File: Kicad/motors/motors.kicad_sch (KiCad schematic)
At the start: 6 parts

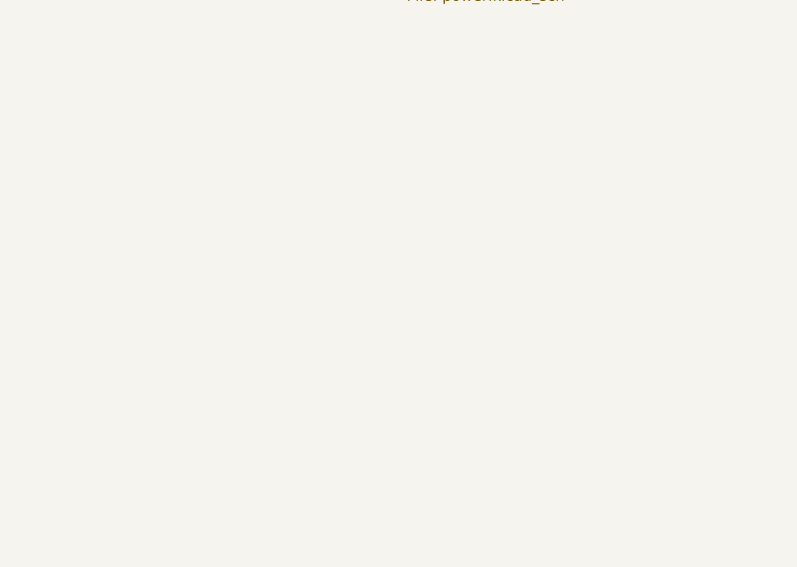
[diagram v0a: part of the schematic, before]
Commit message: Update Motors
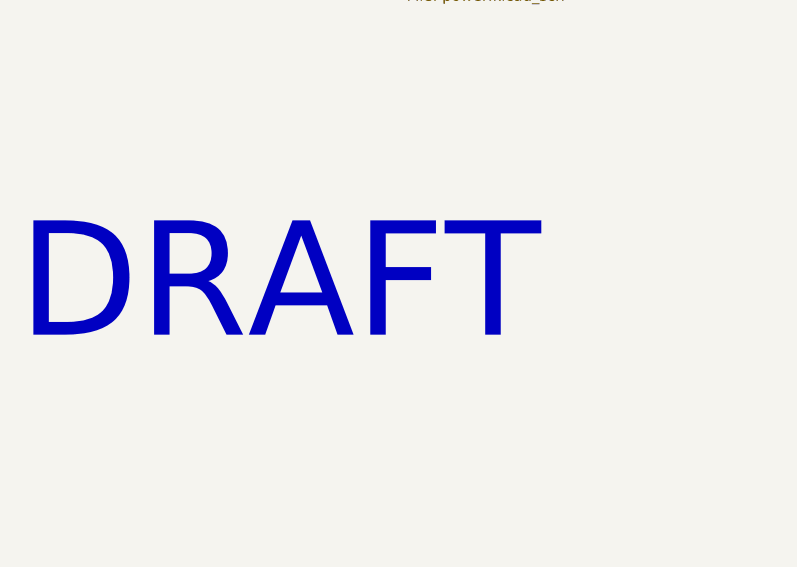
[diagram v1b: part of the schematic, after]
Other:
- note added: "DRAFT"
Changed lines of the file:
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@@
     (comment 1 "TCAR Motor Board - L298P")
+  )
+  (text "DRAFT" (at 66.04 137.16 0)
+    (effects (font (size 12.7 12.7)) (justify left bottom))
   )
   (symbol (lib_id "tronixio:MOUNTING-HOLE-MASK-3MM") (at 276.86 172.72 0) (unit 1)

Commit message: Update Motor
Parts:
- added H? (x10): MOUNTING-HOLE-MASK-3MM, tronixio:M3-MASK, symbol tronixio:MOUNTING-HOLE-MASK-3MM

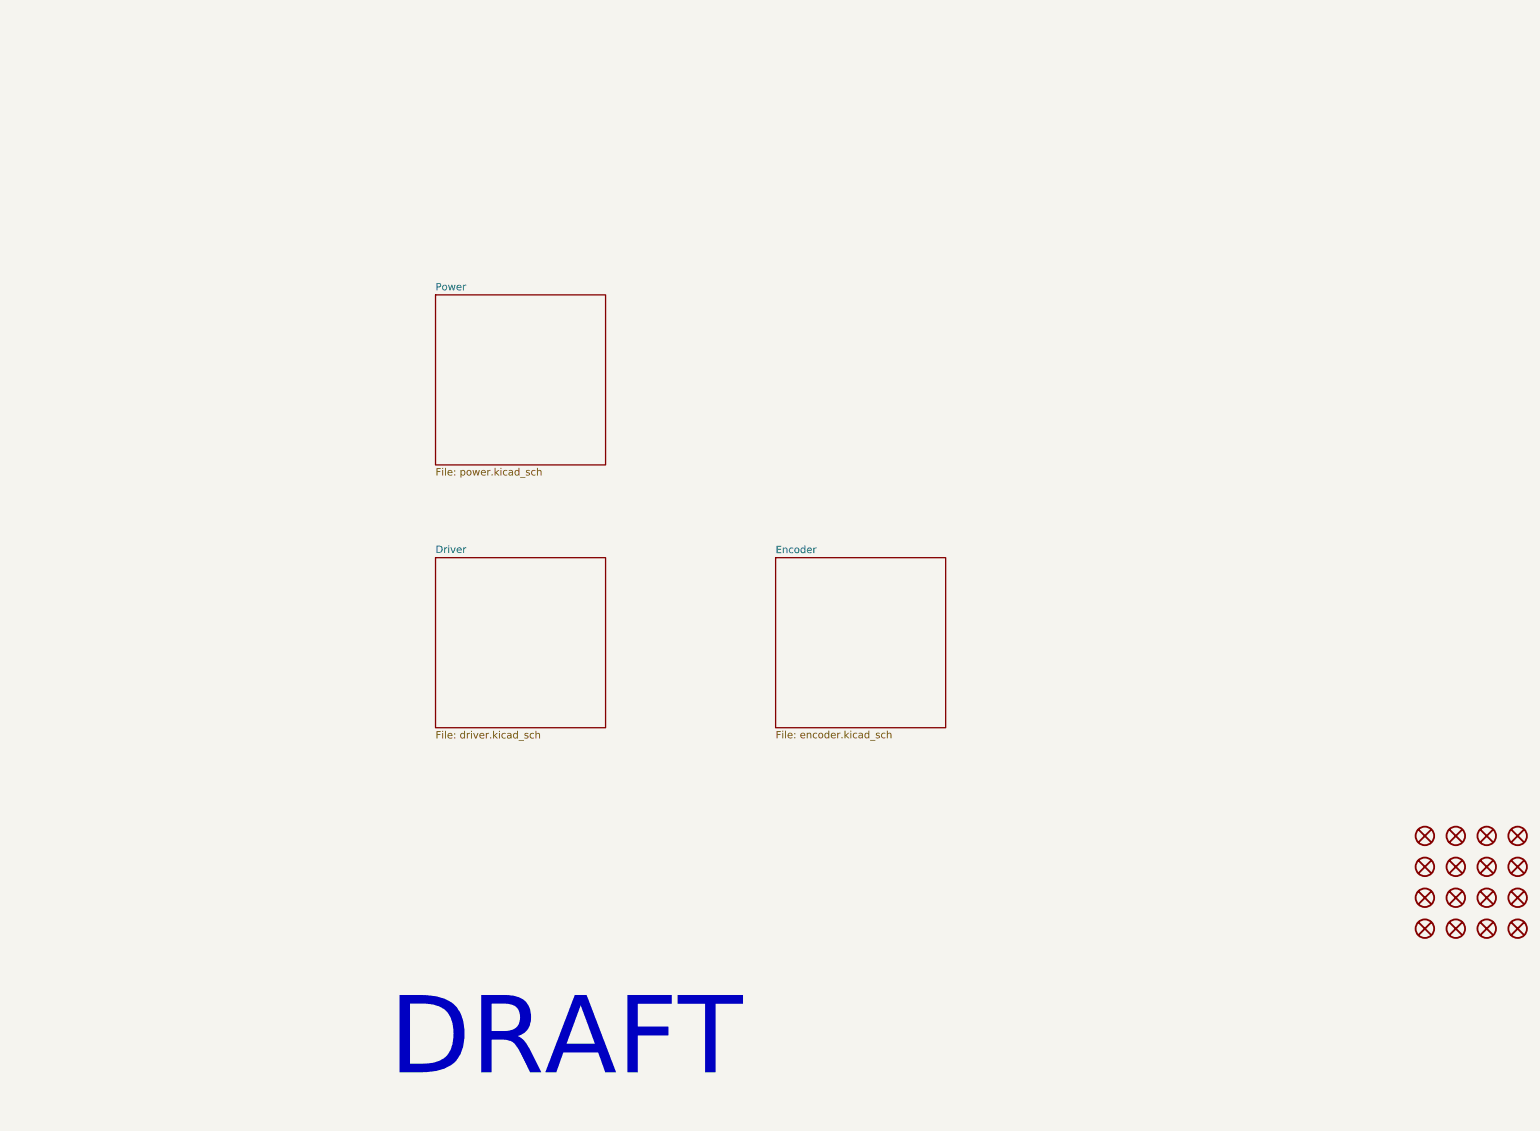
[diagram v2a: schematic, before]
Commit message: Update Motors
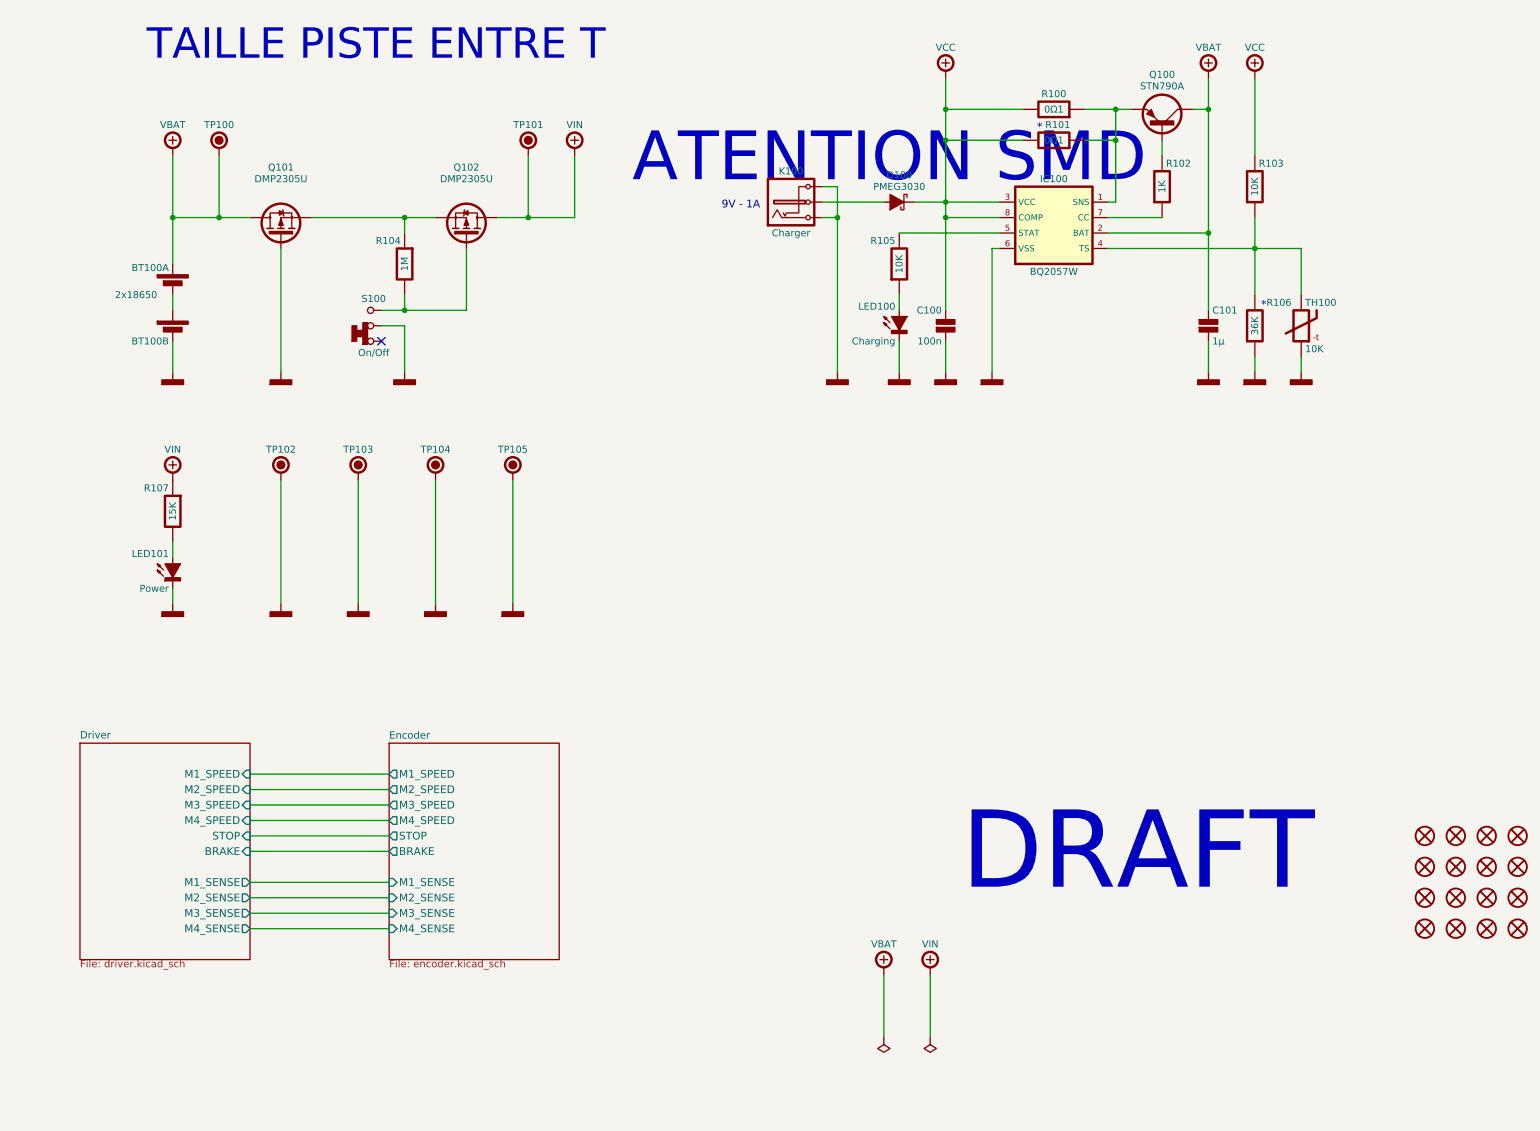
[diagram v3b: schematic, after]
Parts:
- added BT100: 2x18650, tronixio:KEYSTONE-1049, symbol tronixio:KEYSTONE-1049
- added C100: 100n, tronixio:CAPACITOR-1206, symbol tronixio:C-1206
- added C101: 1µ, tronixio:CAPACITOR-1206, symbol tronixio:C-1206
- added D100: PMEG3030, tronixio:SOD-128, symbol tronixio:PMEG3030
- added IC100: BQ2057W, tronixio:SOIC-08, symbol tronixio:BQ2057W
- added K100: Charger, tronixio:CUI-PJ-102AH, symbol tronixio:CUI-PJ-102AH-TH
- added LED100: Charging, tronixio:LED-1206, symbol tronixio:LED-1206-RED
- added LED101: Power, tronixio:LED-1206, symbol tronixio:LED-1206-RED
- added Q100: STN790A, tronixio:SOT-223-3, symbol tronixio:STN790A
- added Q101, Q102: DMP2305U, tronixio:SOT-23-3, symbol tronixio:DMP2305U-NEW
- added R100, R101: 0Ω1, tronixio:RESISTOR-1210, symbol tronixio:R-1210
- added R102: 1K, tronixio:RESISTOR-1206, symbol tronixio:R-1206
- added R103, R105: 10K, tronixio:RESISTOR-1206, symbol tronixio:R-1206
- added R104: 1M, tronixio:RESISTOR-1206, symbol tronixio:R-1206
- added R106: 36K, tronixio:RESISTOR-1206, symbol tronixio:R-1206
- added R107: 15K, tronixio:RESISTOR-1206, symbol tronixio:R-1206
- added S100: On/Off, tronixio:zzzE-SWITCH-200USPXT1A1M6RE, symbol tronixio:E-SWITCH-200USP1T1A1M6RE
- added TH100: 10K, tronixio:THERMISTOR, symbol tronixio:THERMISTOR-NTC-10K
- added TP100, TP101, TP102, TP103, TP104, TP105: HARWIN-S1751, tronixio:zzzHARWIN-S1751, symbol tronixio:HARWIN-S1751
- gave numbers to parts that had none: 16
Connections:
- new net: Q102.1 (G), R104.1, S100.3
- new net: Q100.1 (B), R102.1
- new net: IC100.1 (SNS), Q100.3 (E), R100.2, R101.2
- new net: BT100.1 (-), BT100.4 (+)
- new net: Q101.2 (S), Q102.2 (S), R104.2
- new net: D100.2 (A), K100.1
- new net: LED101.2 (A), R107.1
- new net: IC100.4 (TS), R103.2, R106.1, TH100.1
- new net: IC100.7 (CC), R102.2
- new net: IC100.5 (STAT), R105.1
- new net: LED100.2 (A), R105.2
- new net GND: BT100.3 (-), C100.2, C101.2, IC100.6 (VSS), K100.2, K100.3, LED100.1 (K), LED101.1 (K), Q101.1 (G), R106.2, S100.2, TH100.2, TP102.1, TP103.1, TP104.1, TP105.1
- new net VBAT: BT100.2 (+), C101.1, IC100.2 (BAT), Q100.2 (C), Q101.3 (D), TP100.1
- new net VCC: C100.1, D100.1 (C), IC100.3 (VCC), IC100.8 (COMP), R100.1, R101.1, R103.1
- new net VIN: Q102.3 (D), R107.2, TP101.1
- no-connect marks 0 -> 1
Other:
- removed sheet Power
- sheet Driver ports: added BRAKE, M1_SENSE, M1_SPEED, M2_SENSE, M2_SPEED, M3_SENSE, M3_SPEED, M4_SENSE, M4_SPEED, STOP; removed none
- sheet Encoder ports: added BRAKE, M1_SENSE, M1_SPEED, M2_SENSE, M2_SPEED, M3_SENSE, M3_SPEED, M4_SENSE, M4_SPEED, STOP; removed none
- note added: "*"
- note added: "9V - 1A"
- note added: "ATENTION SMD"
- note added: "TAILLE PISTE ENTRE T"

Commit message: Update Motor
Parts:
- removed Q101, Q102: DMP2305U, tronixio:SOT-23-3, symbol tronixio:DMP2305U-NEW
- removed TP104, TP105: HARWIN-S1751, tronixio:zzzHARWIN-S1751, symbol tronixio:HARWIN-S1751
- added H117, H118, H119, H120: MOUNTING-HOLE-MASK-3MM, tronixio:M3.5, symbol tronixio:MOUNTING-HOLE-3.5MM
- added T101, T102: DMP2305U, tronixio:SOT-23-3, symbol tronixio:DMP2305U
- K100: footprint tronixio:CUI-PJ-102AH -> tronixio:zzzCUI-PJ-002AH-SMT-TR; symbol tronixio:CUI-PJ-102AH-TH -> tronixio:CUI-PJ-002AH-SMT-TR; MOUSER 490-PJ-102AH -> 490-PJ-002AH-SMT-TR
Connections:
- net GND: now also T101.1 (G)
- net VBAT: now also T101.3 (D)
- net VIN: now also T102.3 (D)
- net at R104.1, S100.3: now also T102.1 (G)
- net at R104.2: now also T101.2 (S), T102.2 (S)
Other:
- note removed: "ATENTION SMD"
- note removed: "TAILLE PISTE ENTRE T"
- moved on the sheet: LED101, R107, TP102, TP103

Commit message: Update
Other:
- title: Diagram -> Power
- moved on the sheet: BT100A, BT100B, C100, C101, D100, IC100, K100, LED100, LED101, Q100, R100, R101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

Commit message: Update Motor
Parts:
- BT100: value 2x18650 -> (none); MOUSER 534-1049 -> (none); Mouser (none) -> 534-1049
- D100: symbol tronixio:PMEG3030 -> tronixio:NEXPERIA-PMEG3030; MOUSER 771-PMEG3030EP115 -> (none); Mouser (none) -> 771-PMEG3030EP115; Name (none) -> PMEG3030
- IC100: value BQ2057W -> (none); symbol tronixio:BQ2057W -> tronixio:TI-BQ2057W; MOUSER 595-BQ2057WSN -> (none); Mouser (none) -> 595-BQ2057WSN; Name (none) -> BQ2057W
- K100: footprint tronixio:zzzCUI-PJ-002AH-SMT-TR -> (none); MOUSER 490-PJ-002AH-SMT-TR -> (none); Mouser (none) -> 490-PJ-002AH-SMT-TR
- LED100, LED101: MOUSER 604-APT3216LSECKJ3RV -> (none); Mouser (none) -> 604-APT3216LSECKJ3RV
- Q100: renamed from T101; value DMP2305U -> (none); symbol tronixio:DMP2305U -> tronixio:DIODESINC-DMP2305U-SOT-23; MOUSER 621-DMP2305U-7 -> (none); Mouser (none) -> 621-DMP2305U-7; Name (none) -> DMP2305U
- Q101: renamed from T102; value DMP2305U -> (none); symbol tronixio:DMP2305U -> tronixio:DIODESINC-DMP2305U-SOT-23; MOUSER 621-DMP2305U-7 -> (none); Mouser (none) -> 621-DMP2305U-7; Name (none) -> DMP2305U
- Q102: renamed from Q100; value STN790A -> (none); symbol tronixio:STN790A -> tronixio:ST-STN790A; MOUSER 511-STN790A -> (none); Mouser (none) -> 511-STN790A; Name (none) -> STN90
- S100: footprint tronixio:zzzE-SWITCH-200USPXT1A1M6RE -> (none); MOUSER 612-200USP1T1A1M6RE -> (none); Mouser (none) -> 612-200USP1T1A1M6RE
- TH100: MOUSER 594-NTCLE213E3103FL -> (none); Mouser (none) -> 594-NTCLE213E3103FL; Name (none) -> 10K
- TP100, TP101, TP102, TP103: footprint tronixio:zzzHARWIN-S1751 -> (none); MOUSER 855-S1751-46 -> (none); Mouser (none) -> 855-S1751-46
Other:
- note added: "R101 (0Ω1): ICharge ~1A."

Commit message: Update
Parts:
- added TP104, TP105: KEYSTONE-2000-3, tronixio:KEYSTONE-2000-3, symbol tronixio:KEYSTONE-2000-3
- BT100: value (none) -> 2x18650
- D100: value PMEG3030 -> NEXPERIA-PMEG3030
- IC100: value (none) -> BQ2057W
- K100: footprint (none) -> tronixio:CUI-PJ-002AH-SMT-TR
- LED100: value Charging -> LED-1206-RED; Name (none) -> Red
- LED101: value Power -> LED-1206-RED; Name (none) -> Red
- Q100, Q101: value (none) -> DIODESINC-DMP2305U-SOT-23
- Q102: value (none) -> ST-STN790A
- S100: footprint (none) -> tronixio:zzzE-SWITCH-200USPXT1A1M6RE
- TP100: footprint (none) -> tronixio:HARWIN-S1751; Name (none) -> VBAT
- TP101: footprint (none) -> tronixio:HARWIN-S1751; Name (none) -> VIN
- TP102, TP103: footprint (none) -> tronixio:HARWIN-S1751; Name (none) -> GND
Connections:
- net GND: now also TP104.1, TP105.1
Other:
- note added: "*R101: Optional, needed for adjust precise value."
- note added: "*R106: 10K if NTC TH100 Not Populate."
- note added: "R100 (0Ω1): ICharge ~1A."
- note removed: "R101 (0Ω1): ICharge ~1A."
- moved on the sheet: BT100A, BT100B, C100, C101, D100, IC100, K100, LED100, LED101, Q100, Q101, Q102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
